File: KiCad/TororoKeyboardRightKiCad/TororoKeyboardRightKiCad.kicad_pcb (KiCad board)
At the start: 2 copper layers, 163.4 x 99.3 mm, 112 parts, among them J1 MJ-4PP-9, SW1 SW_PUSH, SW10 SW_PUSH, SW11 SW_PUSH, SW12 SW_PUSH, SW13 SW_PUSH, SW14 SW_PUSH, SW15 SW_PUSH, SW16 SW_PUSH, SW17 SW_PUSH, SW18 SW_PUSH, SW19 SW_PUSH, SW2 SW_PUSH, SW20 SW_PUSH, SW21 SW_PUSH, SW22 SW_PUSH, SW23 SW_PUSH, SW24 SW_PUSH, SW25 SW_PUSH, SW26 SW_PUSH, SW27 SW_PUSH, SW28 SW_PUSH, SW29 SW_PUSH, SW3 SW_PUSH, SW30 SW_PUSH, SW31 SW_PUSH, SW32 SW_PUSH, SW33 SW_PUSH, SW34 SW_PUSH, SW4 SW_PUSH, SW5 SW_PUSH, SW6 SW_PUSH, SW7 SW_PUSH, SW8 SW_PUSH, SW9 SW_PUSH, U1 ProMicro

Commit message: pro micro のフットプリントを右手用に修正してレイアウトを更新
文字の位置を変更した。
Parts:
- U1: footprint kbd_tororo:ProMicro_v2_back -> kbd_tororo:ProMicro_v2_back_right

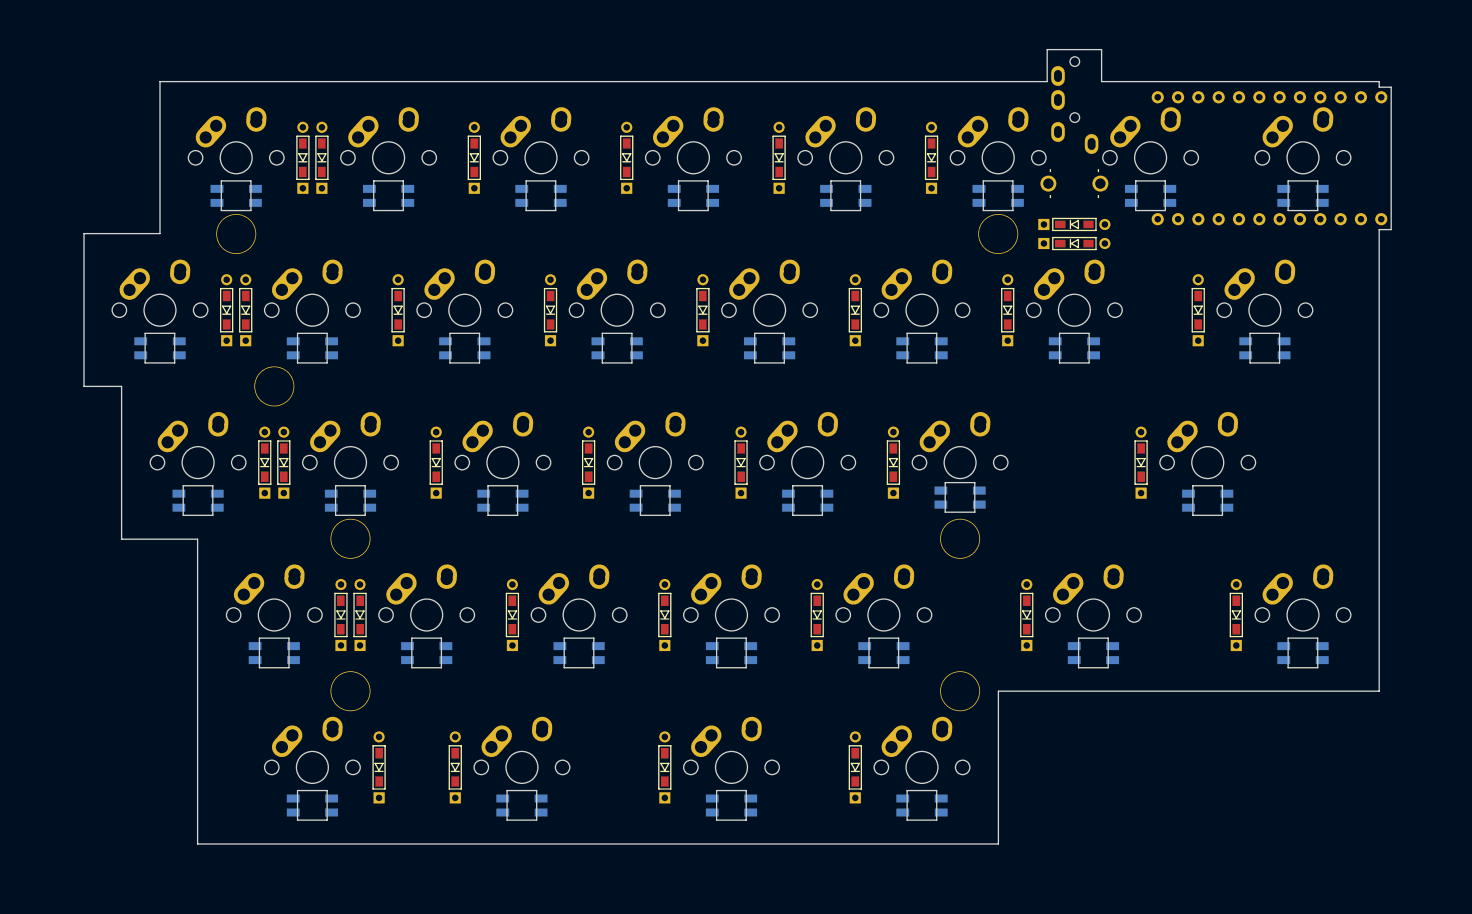
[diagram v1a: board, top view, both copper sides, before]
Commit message: 右手側の配線を整理
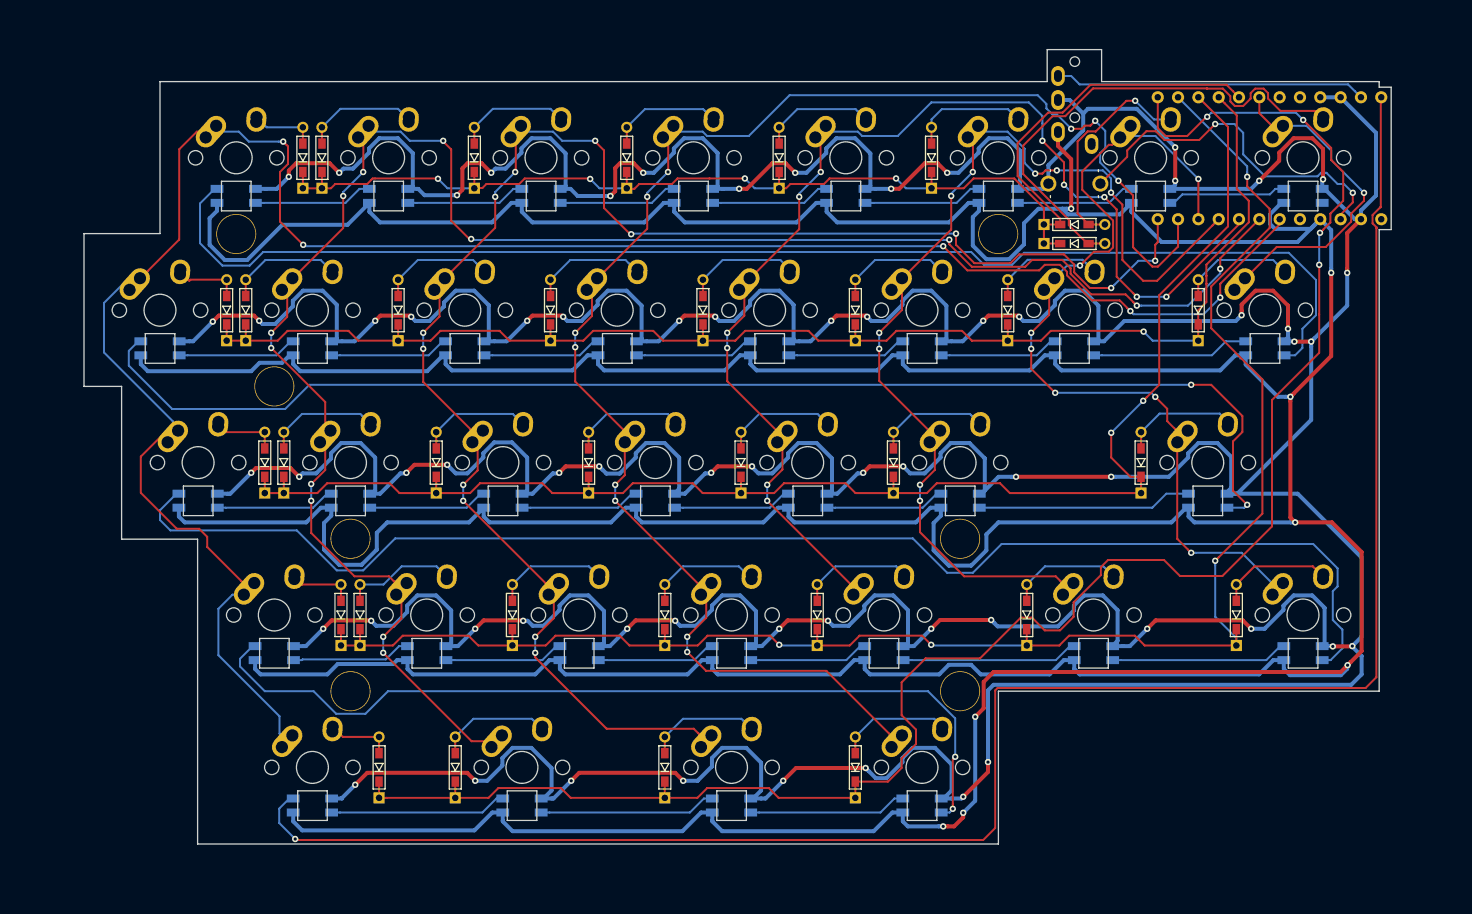
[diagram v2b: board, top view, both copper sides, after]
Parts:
- moved L27 0.39 mm to (138.1, 90.5), turned to 180 degrees
- turned L1 to 180 degrees
- turned L10 to 180 degrees
- turned L11 to 180 degrees
- turned L12 to 180 degrees
- turned L13 to 180 degrees
- turned L14 to 180 degrees
- turned L15 to 180 degrees
- turned L16 to 180 degrees
- turned L17 to 180 degrees
- turned L18 to 180 degrees
- turned L19 to 180 degrees
- turned L2 to 180 degrees
- turned L20 to 180 degrees
- turned L21 to 180 degrees
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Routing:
- net GND: track 0.00 -> 1083.9 mm, vias 0 -> 65
- net VCC: track 0.00 -> 907.4 mm, vias 0 -> 8
- net col8: track 0.00 -> 261.0 mm, vias 0 -> 5
- net led: track 0.00 -> 233.8 mm, vias 0 -> 1
- net col7: track 0.00 -> 233.7 mm, vias 0 -> 13
- net row5: track 0.00 -> 228.0 mm, vias 0 -> 4
- net row4: track 0.00 -> 213.7 mm, vias 0 -> 4
- net col6: track 0.00 -> 206.1 mm, vias 0 -> 13
- net col5: track 0.00 -> 196.8 mm, vias 0 -> 11
- net row3: track 0.00 -> 186.2 mm, vias 0 -> 2
- net row2: track 0.00 -> 176.3 mm, vias 0 -> 1
- net Net-(L3-Pad3): track 0.00 -> 174.3 mm
- net Net-(L1-Pad3): track 0.00 -> 163.8 mm
- net Net-(L2-Pad3): track 0.00 -> 163.2 mm, vias 0 -> 2
- net row1: track 0.00 -> 163.1 mm, vias 0 -> 4
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
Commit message: GNDを塗りつぶし
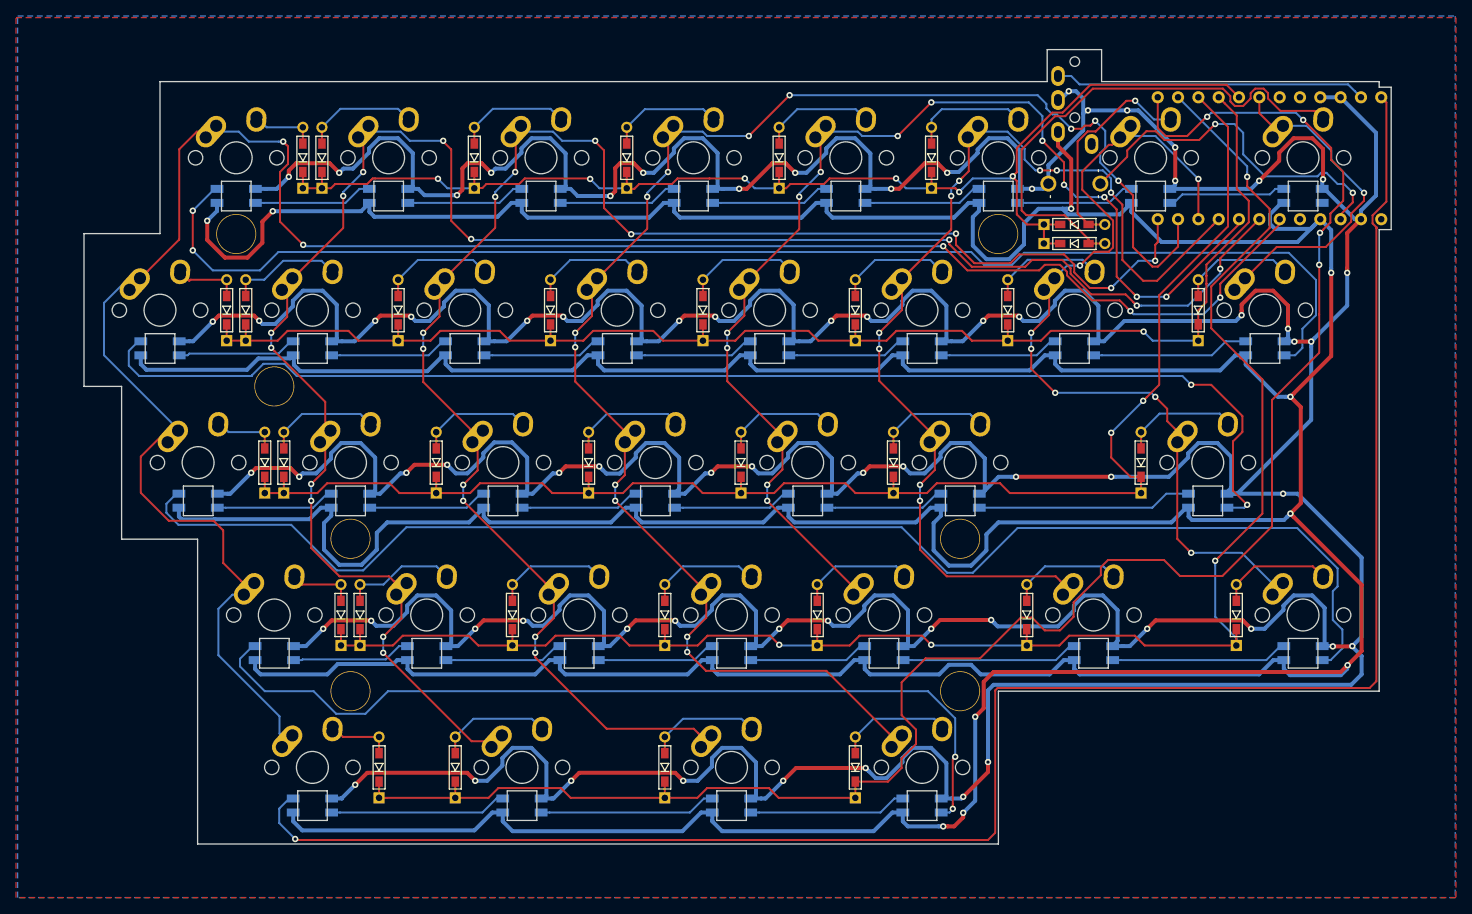
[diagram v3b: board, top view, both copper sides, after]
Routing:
- net row1: track 163.1 -> 157.2 mm, vias 4 -> 6
- net VCC: track 907.4 -> 904.3 mm, vias 8 -> 10
- net Net-(D33-Pad2): track 62.8 -> 65.5 mm
- net Net-(L1-Pad3): track 163.8 -> 166.1 mm, vias 0 -> 2
- net col8: track 261.0 -> 262.6 mm
- net Net-(L2-Pad3): track 163.2 -> 161.9 mm
- net Net-(L3-Pad3): track 174.3 -> 175.5 mm
- net led: track 233.8 -> 235.0 mm
- net col7: track 233.7 -> 234.8 mm
- net GND: track 1083.9 -> 1083.1 mm, vias 65 -> 70
- net col3: track 129.3 -> 130.0 mm
- net col5: vias 11 -> 13
- net col4: vias 11 -> 13
- added copper zone on B.Cu, net GND
- added copper zone on F.Cu, net GND

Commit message: キーボード名とクレジットを配置
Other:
- board text added: "tororo60 right v0.1.0 PCB Designed by katatoshi"
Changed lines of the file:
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@@
   (general
     (thickness 1.6)
-    (drawings 285)
+    (drawings 286)
     (tracks 1971)
     (zones 0)
@@
       (net 87 col1))
   )
+  (gr_text "tororo60 right v0.1.0\nPCB Designed by katatoshi" (at 186.2 82.5 270) (layer B.Mask)
+    (effects (font (size 1 1) (thickness 0.15)) (justify mirror))
+  )
   (gr_line (start 192 56.6) (end 190.5 56.6) (layer Edge.Cuts) (width 0.05))
